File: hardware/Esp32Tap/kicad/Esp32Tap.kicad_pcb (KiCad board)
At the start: 4 copper layers, 95 x 55 mm, 93 parts, among them J1 430450809, J2 430451010, J3 USB-C_HRO_TYPE-C-31-M-12, K1 G6K-2F-Y-TR DC5, Q1 BC817-40,215, Q2 2N7002, SW1 SKRPACE010, SW2 SKRPACE010, U1 ESP32-S3-WROOM-1-N8, U2 TPS54202DDCR, U3 USBLC6-2SC6, U4 TPS3700DDCR, U5 TPS70950DBVR, U6 SN74LVC2G08DCTR, U7 SN74LVC1G126DBVR

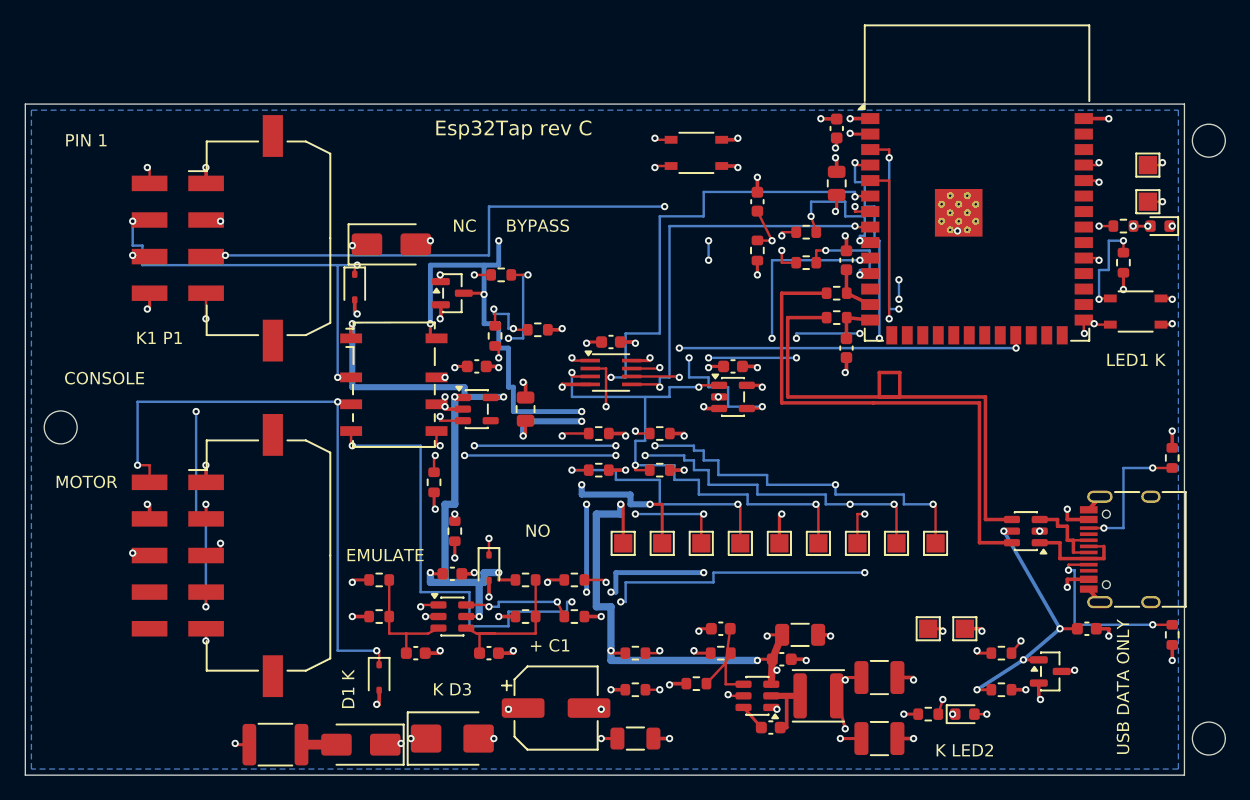
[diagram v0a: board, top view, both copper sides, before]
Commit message: hardware: harden Rev C fabrication proofs
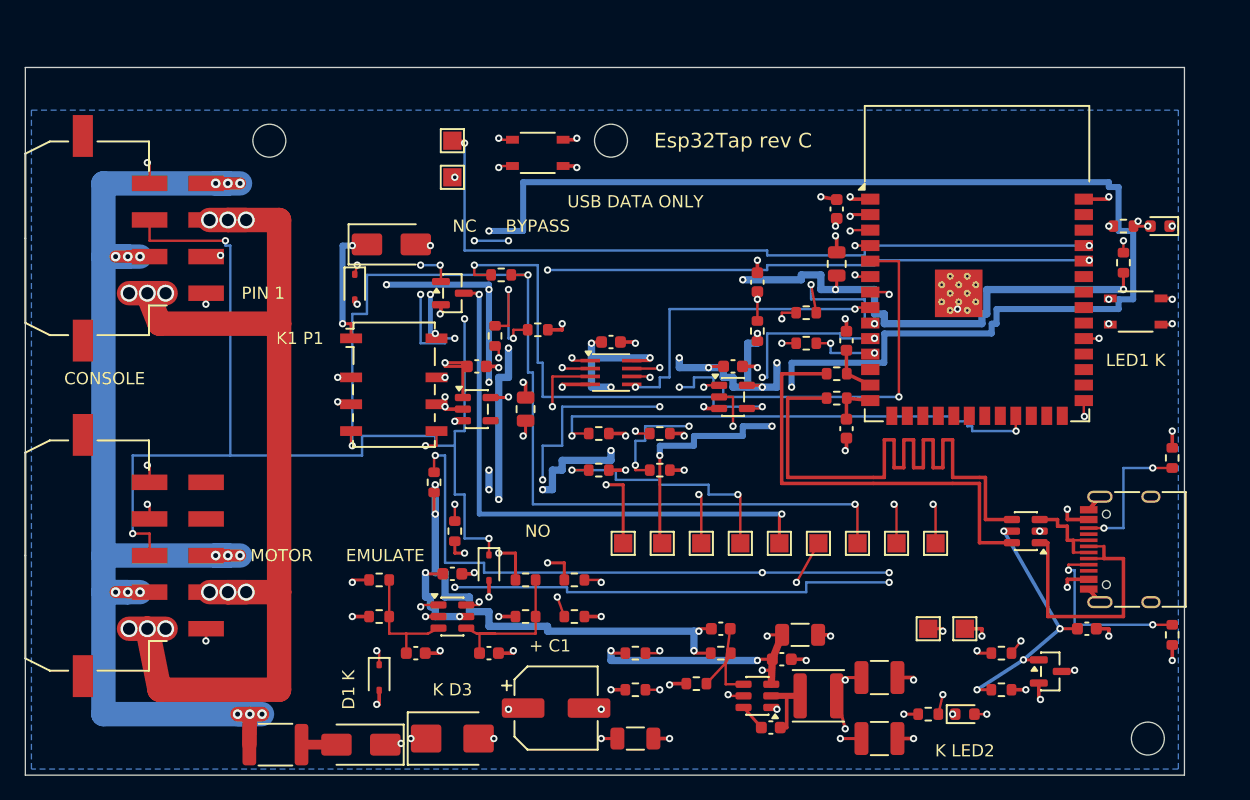
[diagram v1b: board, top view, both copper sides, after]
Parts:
- moved TP1 57.0 mm to (135.0, 103.0)
- moved TP2 57.0 mm to (135.0, 106.0)
- moved MH2 49.0 mm to (148.0, 103.0)
- moved MH1 29.1 mm to (120.0, 103.0)
- moved SW1 13.0 mm to (142.0, 104.0)
- moved C13 6.60 mm to (167.3, 119.4)
- moved C10 6.60 mm to (160.0, 114.6)
- moved C14 6.60 mm to (167.3, 126.6)
- moved C8 6.60 mm to (166.5, 113.1)
- moved C9 6.60 mm to (166.5, 108.6)
- moved R13 6.60 mm to (160.0, 118.6)
- moved R15 6.60 mm to (166.5, 122.1)
- moved R16 6.60 mm to (166.5, 124.1)
- moved R7 6.60 mm to (164.0, 119.6)
- moved R8 6.60 mm to (164.0, 117.1)
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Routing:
- net +5V_RLY: track 58.2 -> 173.2 mm, vias 7 -> 11
- net GND: track 82.4 -> 178.0 mm, vias 59 -> 67
- net U0TXD: track 8.05 -> 62.8 mm
- net U0RXD: track 9.38 -> 61.1 mm, vias 2 -> 5
- net +3V3: track 196.8 -> 238.4 mm, vias 20 -> 29
- net K1_NO_FB: track 88.8 -> 129.6 mm, vias 8 -> 9
- net +8V_RAW: track 68.8 -> 109.5 mm, vias 5 -> 15
- net PIN5_SAFETY: track 50.1 -> 20.5 mm
- net VBUS_PRESENT_N: track 72.1 -> 45.9 mm, vias 5 -> 3
- net VIN: track 133.7 -> 159.2 mm, vias 15 -> 16
- net RELAY_SW: track 84.0 -> 60.2 mm, vias 10 -> 5
- net TX_DRV: track 100.1 -> 80.1 mm, vias 7 -> 3
- net EN: track 69.4 -> 54.2 mm, vias 11 -> 4
- net K1_NC_FB: track 89.0 -> 102.8 mm, vias 9 -> 6
- net TREAD_OK: track 104.0 -> 91.3 mm, vias 10 -> 8
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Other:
- board size 95 x 55 mm -> 95 x 58 mm
